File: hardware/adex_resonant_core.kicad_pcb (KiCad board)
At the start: 4 copper layers, 70 x 70 mm, 286 parts

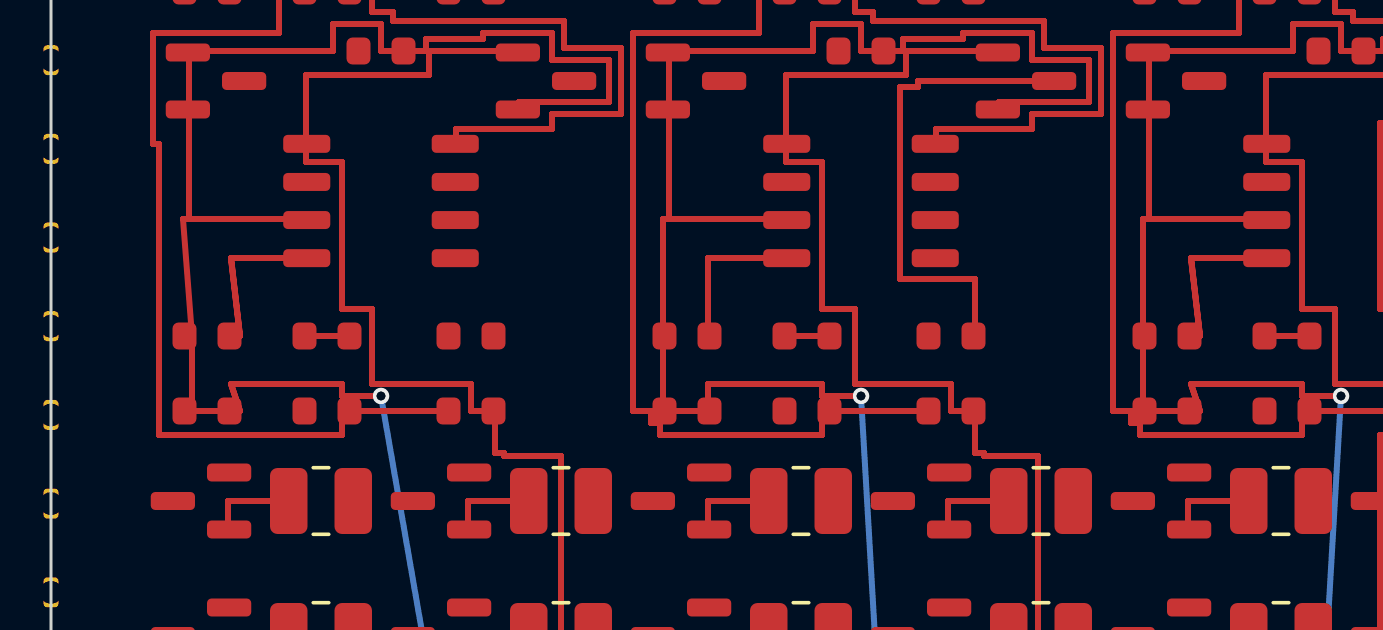
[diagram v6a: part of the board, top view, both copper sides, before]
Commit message: fix(hardware): set solder mask expansion to 0.02mm and resolve aperture bridging DRC errors
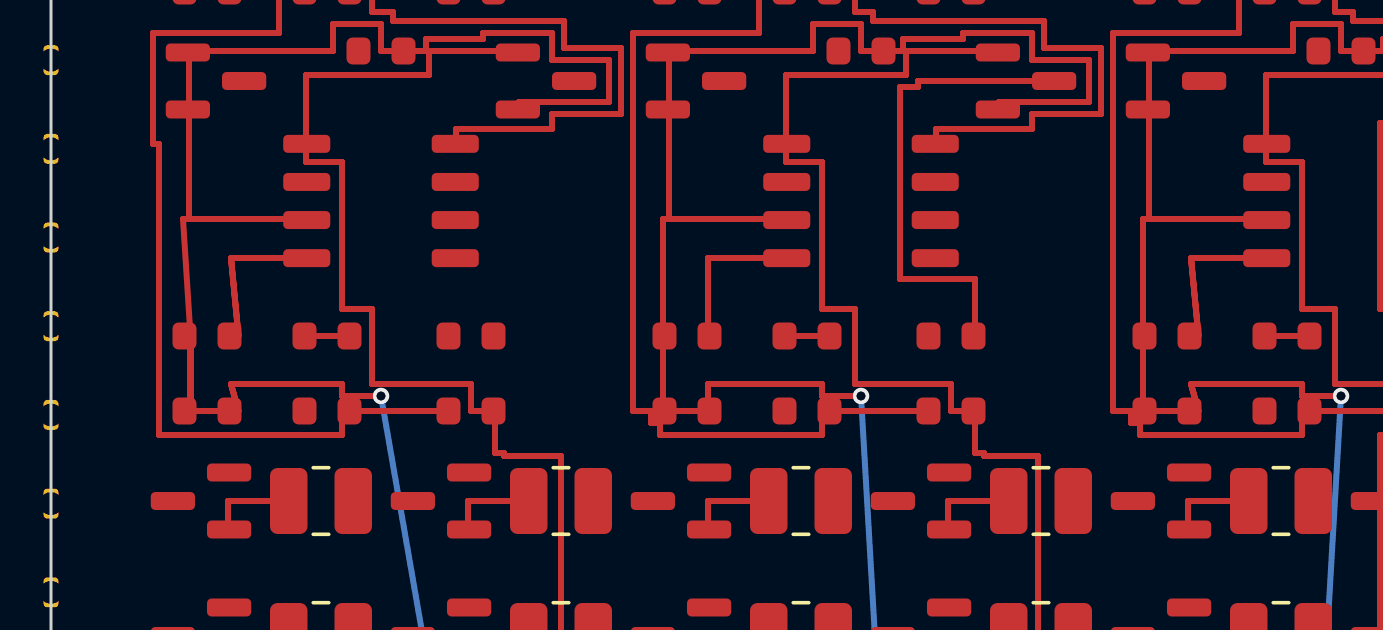
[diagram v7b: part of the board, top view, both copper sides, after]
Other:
- rule pad_to_mask_clearance: -0.05 -> 0.02

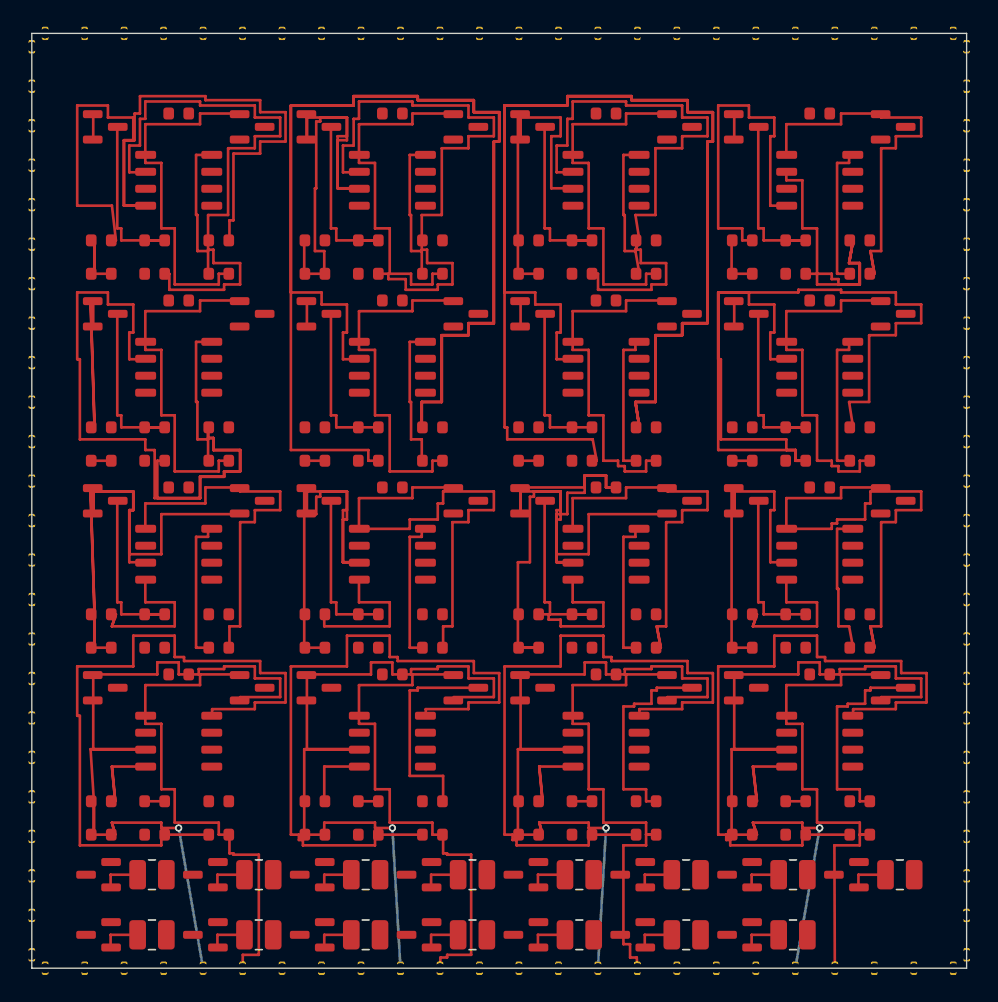
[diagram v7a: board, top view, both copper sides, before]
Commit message: fix(hardware): set solder mask expansion to 0.00mm and enforce perpendicular 0402 trace exits for 0 DRC
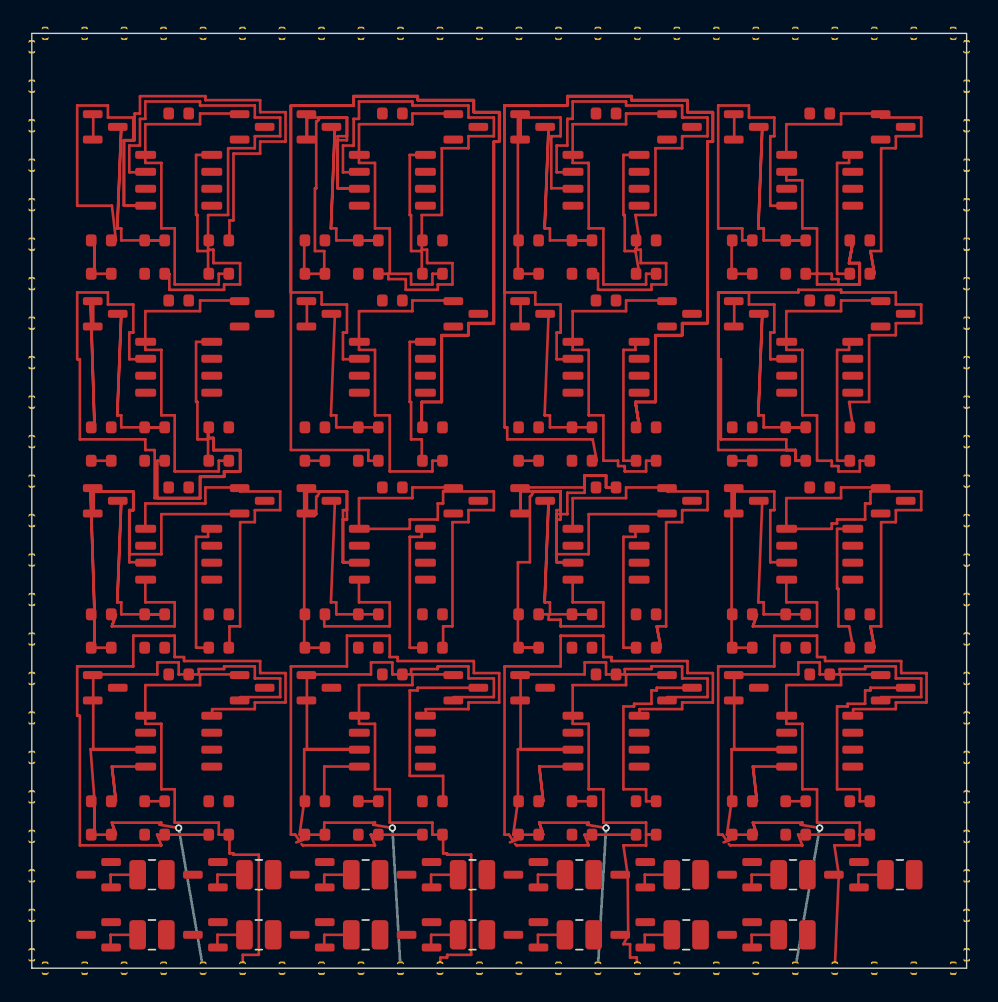
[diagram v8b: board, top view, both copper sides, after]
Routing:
- net N9_VSS: track 13.5 -> 21.1 mm
- net N8_VSS: track 13.7 -> 21.3 mm
- net N5_VSS: track 13.5 -> 21.1 mm
- net N4_VSS: track 13.7 -> 21.3 mm
- net N3_VSS: track 13.7 -> 21.3 mm
- net N2_VSS: track 13.7 -> 21.3 mm
- net N11_VSS: track 13.7 -> 21.3 mm
- net N1_VSS: track 13.5 -> 21.1 mm
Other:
- rule pad_to_mask_clearance: 0.02 -> 0
- rule solder_mask_min_width: 0.08 -> 0.05
